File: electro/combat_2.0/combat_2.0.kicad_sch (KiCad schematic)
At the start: 21 parts, among them J1 BATT, J5 UART, SW1 BOOT, SW2 EN, U2 AZ1117CH-5.0TRG1, U6 LD29150DT33R

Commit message: competition rules
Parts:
- added D3: LED, symbol Device:LED
- added R1: 220, Resistor_SMD:R_1206_3216Metric_Pad1.30x1.75mm_HandSolder, symbol Device:R
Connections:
- net +5V: now also C13.1, U6.3 (IN)
- net +8V: no longer C13.1, U6.3 (IN)
- net ESP32 PCB adapter/IO35: now also D3.2 (A)
- net GND: now also R1.1
- new net: D3.1 (K), R1.2
- no-connect marks 20 -> 18
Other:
- note added: "Competition Rules: Robot must include a mechanism allowing to turn off its drive and weapon safely after loosing connection with a transmitter. Robot must be equipped with a clearly visible, durable weapon lock (e.g. a safety pin crippling a blade) Robot must be equipped with ON/OFF state indicator, clearly visible for a referee in any robot's position and orientation (e.g. high power LED)."
- note added: "This Led Should be visible from outside the robot"
- moved on the sheet: J5

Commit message: almost ready pcb
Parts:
- removed C18: 0.1uF, Capacitor_SMD:C_1206_3216Metric_Pad1.33x1.80mm_HandSolder, symbol Device:C
- removed R8: 10kR, Resistor_SMD:R_1206_3216Metric_Pad1.30x1.75mm_HandSolder, symbol Device:R
- added J2: Conn_01x02_Socket, Connector_PinHeader_2.54mm:PinHeader_1x02_P2.54mm_Vertical, symbol Connector:Conn_01x02_Socket
- added R6: 220, Resistor_THT:R_Axial_DIN0204_L3.6mm_D1.6mm_P7.62mm_Horizontal, symbol Device:R
- C2: renamed from C1; value 10uF -> 22uF; footprint Capacitor_SMD:C_1206_3216Metric_Pad1.33x1.80mm_HandSolder -> Capacitor_SMD:C_0805_2012Metric_Pad1.18x1.45mm_HandSolder
- C4: renamed from C2; footprint Capacitor_SMD:C_1206_3216Metric_Pad1.33x1.80mm_HandSolder -> Capacitor_SMD:C_0805_2012Metric_Pad1.18x1.45mm_HandSolder
- C6: renamed from C13; value 0.33uF -> 1uF; footprint Capacitor_SMD:C_1206_3216Metric_Pad1.33x1.80mm_HandSolder -> (none); symbol Device:C -> Device:C_Small
- C7: renamed from C15; footprint Capacitor_SMD:C_1206_3216Metric_Pad1.33x1.80mm_HandSolder -> Capacitor_SMD:C_0805_2012Metric_Pad1.18x1.45mm_HandSolder
- C8: renamed from C14; value 10uF -> 1uF; footprint Capacitor_SMD:CP_Elec_4x5.4 -> Capacitor_SMD:C_0805_2012Metric_Pad1.18x1.45mm_HandSolder; symbol Device:C_Polarized -> Device:C_Small
- D1: renamed from D2; footprint LED_SMD:LED_1206_3216Metric_Pad1.42x1.75mm_HandSolder -> LED_SMD:LED_PLCC-2_3x2mm_AK
- R4: footprint Resistor_SMD:R_1206_3216Metric_Pad1.30x1.75mm_HandSolder -> Resistor_THT:R_Axial_DIN0204_L3.6mm_D1.6mm_P7.62mm_Horizontal
- U2: renamed from U6; footprint Package_TO_SOT_SMD:TO-252-2 -> Package_TO_SOT_SMD:SOT-353_SC-70-5; symbol Regulator_Linear:LD1086DT33TR -> Regulator_Linear:MIC5366-3.3YC5
- renumbered C16 to C1, C17 to C3, D3 to D2, J5 to J3, R10 to R1, R1 to R2, R9 to R3, SW2 to SW1, SW1 to SW2, U2 to U1
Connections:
- net +3V3: now also U2.5 (VOUT), R6.1; no longer U2.2 (OUT)
- net +5V: now also U2.1 (VIN)
- net ESP32 PCB adapter/IO16: now also R6.2
- net ESP32 PCB adapter/IO35: now also J2.2 (Pin_2); no longer D2.2 (A)
- net GND: now also U2.2 (GND); no longer U2.1 (ADJ/GND)
- net at R2.2: now also J2.1 (Pin_1); no longer D2.1 (K)
- no-connect marks 18 -> 12
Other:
- note added: "Chyba można dać po prostu jeden C ?"
- note added: "Chyba można dać po prostu jeden C Jak będą blisko siebie?"
- moved on the sheet: C1, C3, D1, D2, R1, R2, R3, SW1

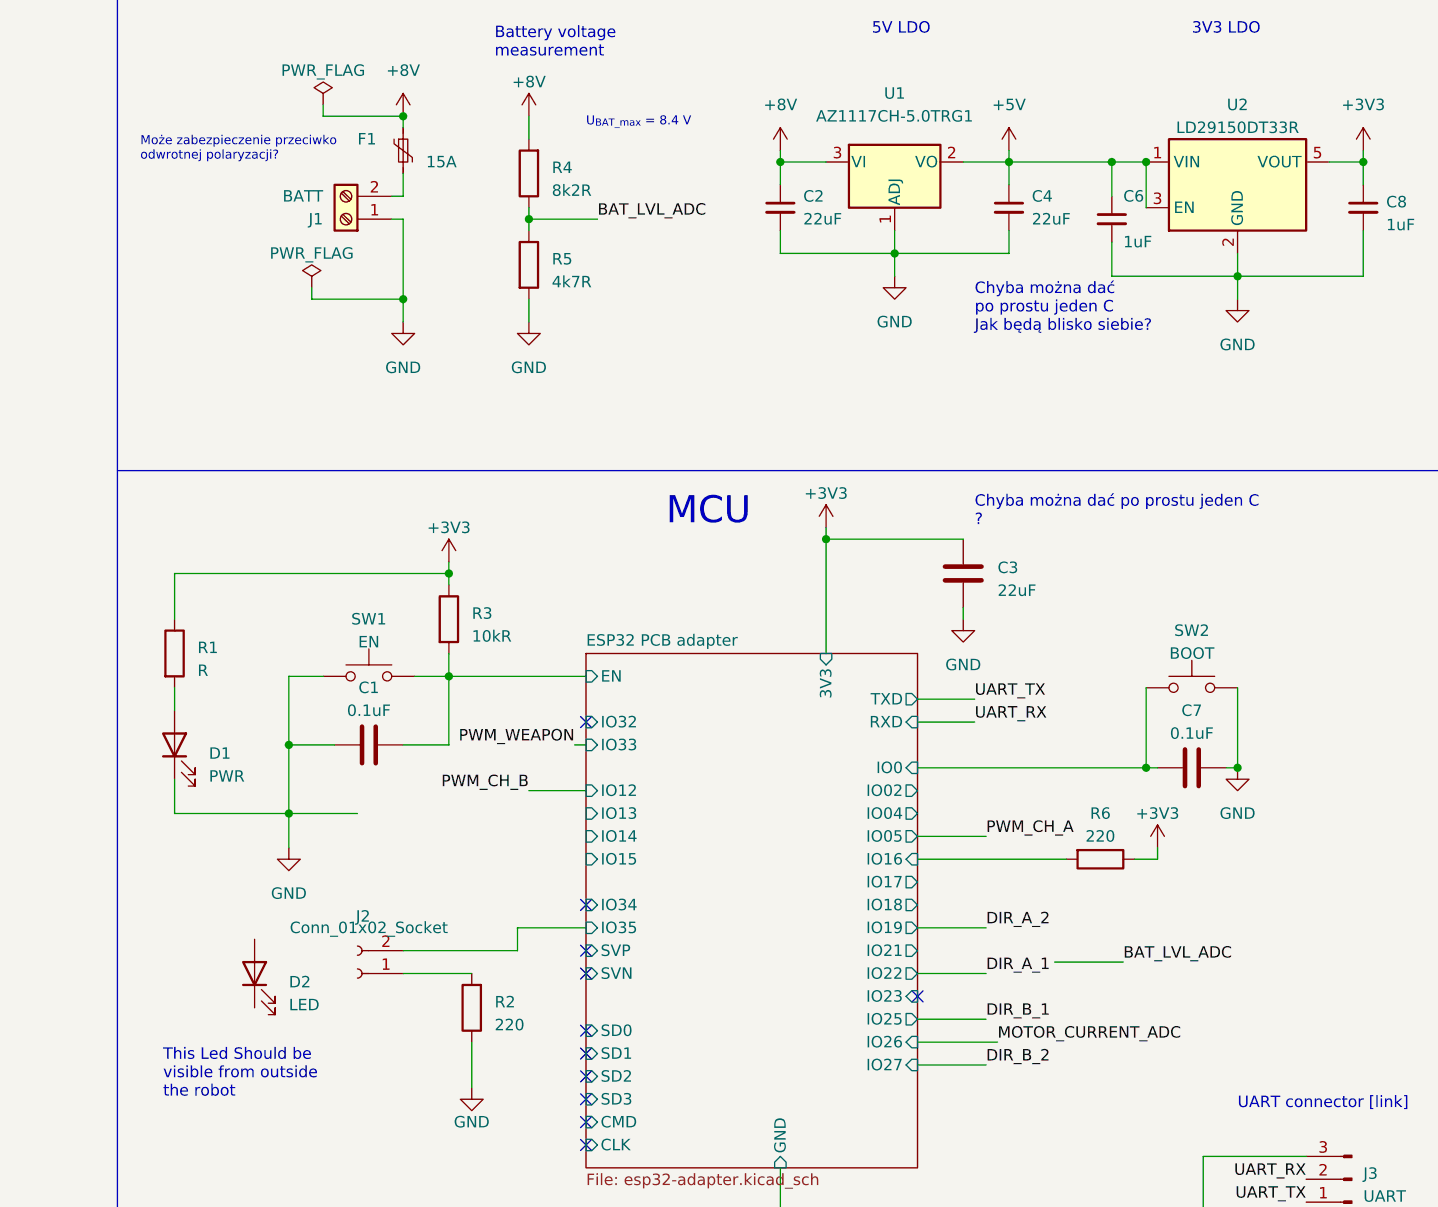
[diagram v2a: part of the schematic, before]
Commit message: Changed pads to ARKs (connecting two boards together), prepared for etching
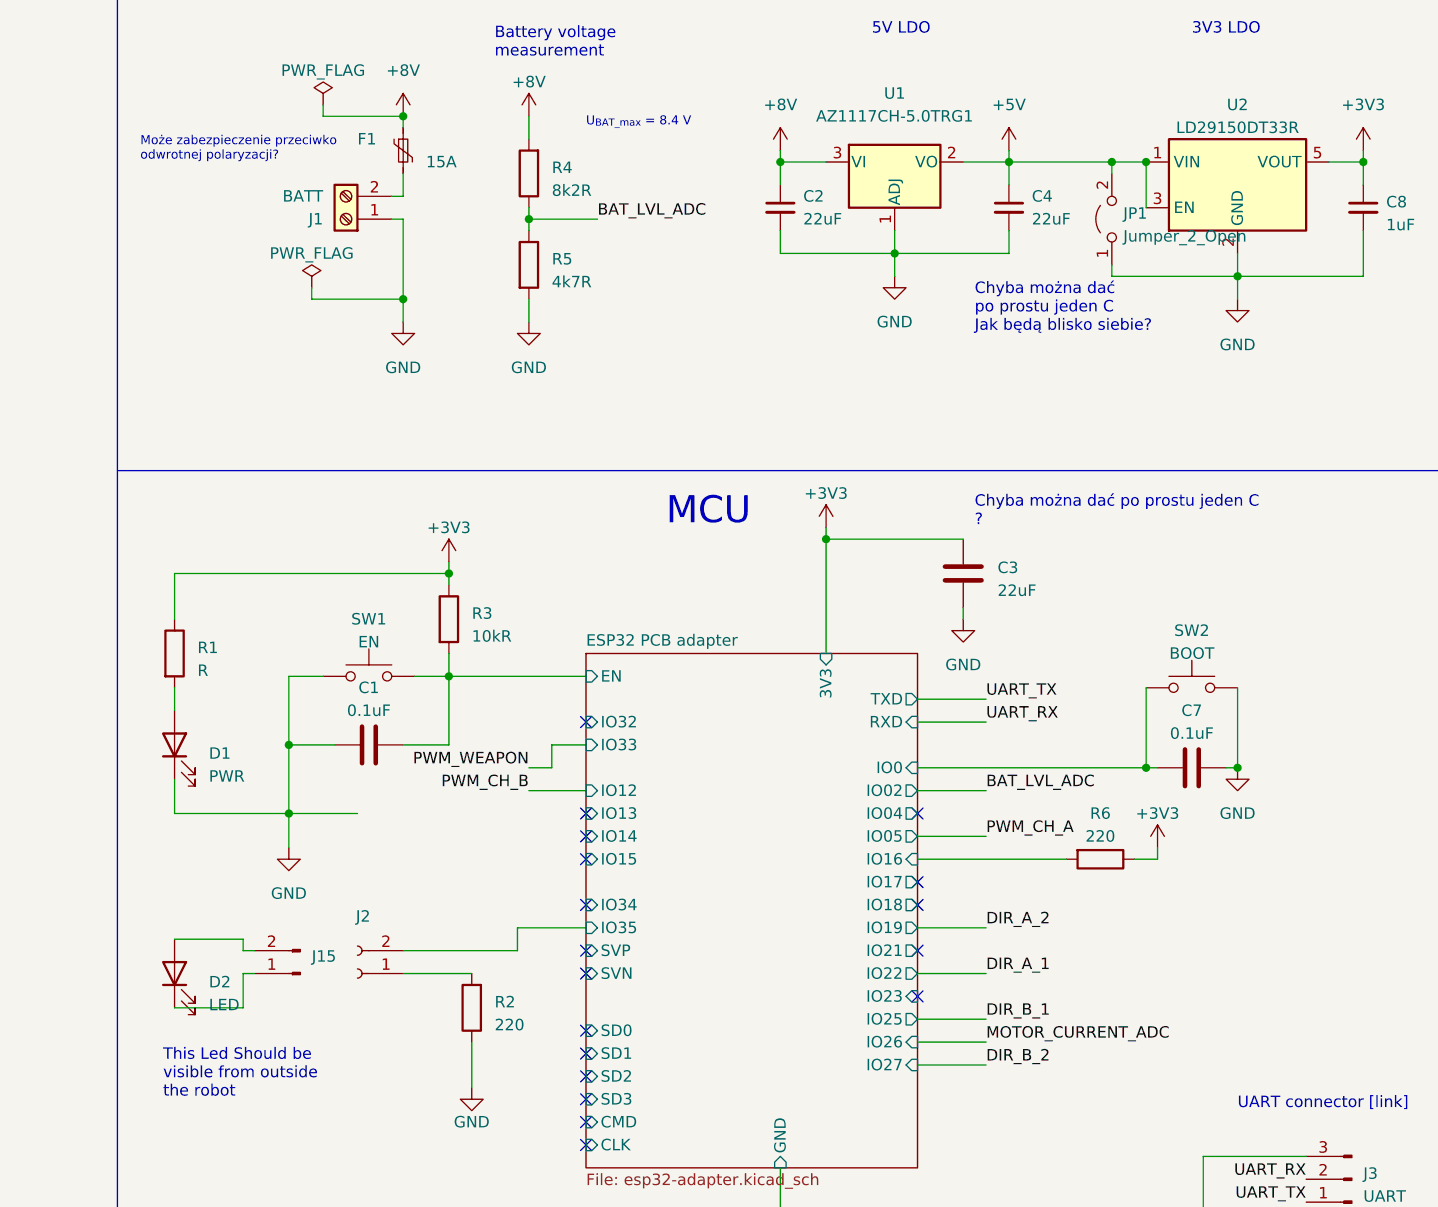
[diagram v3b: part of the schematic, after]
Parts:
- removed C6: 1uF, symbol Device:C_Small
- added J15: Conn_01x02_Pin, symbol Connector:Conn_01x02_Pin
- added JP1: Jumper_2_Open, symbol Jumper:Jumper_2_Open
- R4: footprint Resistor_THT:R_Axial_DIN0204_L3.6mm_D1.6mm_P7.62mm_Horizontal -> Resistor_SMD:R_1206_3216Metric_Pad1.30x1.75mm_HandSolder
- SW1, SW2: now left out of the parts list
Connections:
- net +5V: now also JP1.2 (B)
- net GND: now also JP1.1 (A)
- net at D2.1 (K): now also J15.1 (Pin_1)
- net at D2.2 (A): now also J15.2 (Pin_2)
- no-connect marks 12 -> 19
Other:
- moved on the sheet: D2
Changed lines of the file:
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@@
   (no_connect (at 245.11 48.26))
   (no_connect (at 111.76 147.32))
+  (no_connect (at 74.93 127))
+  (no_connect (at 111.76 127))
   (no_connect (at 74.93 142.24))
   (no_connect (at 74.93 153.67))
@@
   (no_connect (at 74.93 137.16))
   (no_connect (at 74.93 144.78))
+  (no_connect (at 111.76 142.24))
+  (no_connect (at 111.76 134.62))
   (no_connect (at 74.93 163.83))
+  (no_connect (at 74.93 129.54))
+  (no_connect (at 111.76 137.16))
+  (no_connect (at 74.93 132.08))
   (no_connect (at 74.93 151.13))
   (no_connect (at 74.93 156.21))
@@
     (stroke (width 0) (type default))
   )
+  (wire (pts (xy 29.21 148.59) (xy 36.83 148.59))
+    (stroke (width 0) (type default))
+  )
   (wire (pts (xy 212.09 48.26) (xy 204.47 48.26))
     (stroke (width 0) (type default))
@@
     (stroke (width 0) (type default))
   )
-  (wire (pts (xy 111.76 116.84) (xy 118.11 116.84))
+  (wire (pts (xy 111.76 116.84) (xy 119.38 116.84))
     (stroke (width 0) (type default))
   )
@@
     (stroke (width 0) (type default))
   )
-  (wire (pts (xy 127 143.51) (xy 134.62 143.51))
+  (wire (pts (xy 111.76 124.46) (xy 119.38 124.46))
     (stroke (width 0) (type default))
   )
@@
     (stroke (width 0) (type default))
   )
-  (wire (pts (xy 133.35 54.61) (xy 133.35 58.42))
+  (wire (pts (xy 133.35 54.61) (xy 133.35 55.88))
     (stroke (width 0) (type default))
   )
@@
     (stroke (width 0) (type default))
   )
+  (wire (pts (xy 71.12 121.92) (xy 71.12 119.38))
+    (stroke (width 0) (type default))
+  )
   (wire (pts (xy 147.32 67.31) (xy 161.29 67.31))
     (stroke (width 0) (type default))
@@
     (stroke (width 0) (type default))
   )
-  (wire (pts (xy 111.76 152.4) (xy 120.65 152.4))
+  (wire (pts (xy 111.76 152.4) (xy 119.38 152.4))
     (stroke (width 0) (type default))
   )
@@
     (stroke (width 0) (type default))
   )
+  (wire (pts (xy 36.83 144.78) (xy 38.1 144.78))
+    (stroke (width 0) (type default))
+  )
   (wire (pts (xy 242.57 125.73) (xy 245.11 125.73))
     (stroke (width 0) (type default))
@@
     (stroke (width 0) (type default))
   )
-  (wire (pts (xy 133.35 63.5) (xy 133.35 67.31))
-    (stroke (width 0) (type default))
-  )
   (wire (pts (xy 62.23 152.4) (xy 62.23 157.48))
     (stroke (width 0) (type default))
   )
-  (wire (pts (xy 74.93 119.38) (xy 73.66 119.38))
+  (wire (pts (xy 71.12 121.92) (xy 68.58 121.92))
     (stroke (width 0) (type default))
   )
@@
     (stroke (width 0) (type default))
   )
+  (wire (pts (xy 29.21 140.97) (xy 36.83 140.97))
+    (stroke (width 0) (type default))
+  )
   (polyline (pts (xy 274.32 157.48) (xy 274.32 19.05))
     (stroke (width 0) (type default))
@@
     (stroke (width 0) (type default))
   )
+  (wire (pts (xy 36.83 142.24) (xy 38.1 142.24))
+    (stroke (width 0) (type default))
+  )
   (wire (pts (xy 111.76 132.08) (xy 128.27 132.08))
     (stroke (width 0) (type default))
@@
     (stroke (width 0) (type default))
   )
+  (wire (pts (xy 133.35 66.04) (xy 133.35 67.31))
+    (stroke (width 0) (type default))
+  )
   (wire (pts (xy 205.74 133.35) (xy 205.74 137.16))
     (stroke (width 0) (type default))
   )
+  (wire (pts (xy 36.83 148.59) (xy 36.83 144.78))
+    (stroke (width 0) (type default))
+  )
   (wire (pts (xy 241.3 55.88) (xy 243.84 55.88))
     (stroke (width 0) (type default))
   )
-  (wire (pts (xy 111.76 114.3) (xy 118.11 114.3))
+  (wire (pts (xy 111.76 114.3) (xy 119.38 114.3))
     (stroke (width 0) (type default))
   )
@@
   )
   (wire (pts (xy 111.76 129.54) (xy 119.38 129.54))
+    (stroke (width 0) (type default))
+  )
+  (wire (pts (xy 71.12 119.38) (xy 74.93 119.38))
+    (stroke (width 0) (type default))
+  )
+  (wire (pts (xy 36.83 140.97) (xy 36.83 142.24))
     (stroke (width 0) (type default))
   )
@@
     (effects (font (size 1.27 1.27)) (justify left bottom))
   )
-  (label "UART_RX" (at 118.11 116.84 0) (fields_autoplaced)
+  (label "UART_RX" (at 119.38 116.84 0) (fields_autoplaced)
     (effects (font (size 1.27 1.27)) (justify left bottom))
   )
@@
     (effects (font (size 1.27 1.27)) (justify left bottom))
   )
-  (label "MOTOR_CURRENT_ADC" (at 120.65 152.4 0) (fields_autoplaced)
-    (effects (font (size 1.27 1.27)) (justify left bottom))
-  )
-  (label "BAT_LVL_ADC" (at 134.62 143.51 0) (fields_autoplaced)
+  (label "MOTOR_CURRENT_ADC" (at 119.38 152.4 0) (fields_autoplaced)
+    (effects (font (size 1.27 1.27)) (justify left bottom))
+  )
+  (label "BAT_LVL_ADC" (at 119.38 124.46 0) (fields_autoplaced)
     (effects (font (size 1.27 1.27)) (justify left bottom))
   )
@@
     (effects (font (size 1.27 1.27)) (justify left bottom))
   )
-  (label "PWM_WEAPON" (at 73.66 119.38 180) (fields_autoplaced)
+  (label "PWM_WEAPON" (at 68.58 121.92 180) (fields_autoplaced)
     (effects (font (size 1.27 1.27)) (justify right bottom))
   )
-  (label "UART_TX" (at 118.11 114.3 0) (fields_autoplaced)
+  (label "UART_TX" (at 119.38 114.3 0) (fields_autoplaced)
     (effects (font (size 1.27 1.27)) (justify left bottom))
   )
@@
       (effects (font (size 1.27 1.27)) (justify right))
     )
-    (property "Footprint" "Resistor_THT:R_Axial_DIN0204_L3.6mm_D1.6mm_P7.62mm_Horizontal" (at 70.358 55.88 90)
+    (property "Footprint" "Resistor_SMD:R_1206_3216Metric_Pad1.30x1.75mm_HandSolder" (at 70.358 55.88 90)
       (effects (font (size 1.27 1.27)) hide)
     )
@@
   )
   (symbol (lib_id "Switch:SW_Push") (at 50.8 111.76 0) (unit 1)
-    (in_bom yes) (on_board yes) (dnp no) (fields_autoplaced)
+    (in_bom no) (on_board no) (dnp no) (fields_autoplaced)
     (property "Reference" "SW1" (at 50.8 105.41 0)
       (effects (font (size 1.27 1.27)))
@@
     )
   )
+  (symbol (lib_id "Jumper:Jumper_2_Open") (at 133.35 60.96 90) (unit 1)
+    (in_bom no) (on_board no) (dnp no) (fields_autoplaced)
+    (property "Reference" "JP1" (at 134.62 60.325 90)
+      (effects (font (size 1.27 1.27)) (justify right))
+    )
+    (property "Value" "Jumper_2_Open" (at 134.62 62.865 90)
+      (effects (font (size 1.27 1.27)) (justify right))
+    )
+    (property "Footprint" "" (at 133.35 60.96 0)
+      (effects (font (size 1.27 1.27)) hide)
+    )
+    (property "Datasheet" "~" (at 133.35 60.96 0)
+      (effects (font (size 1.27 1.27)) hide)
+    )
+    (pin "1")
+    (pin "2")
+    (instances
+      (project "combat_2.0"
+        (path "/518cdd36-e3d2-496e-a534-90a14dea15b3"
+          (reference "JP1") (unit 1)
+        )
+      )
+    )
+  )
   (symbol (lib_id "Device:C") (at 142.24 121.92 90) (unit 1)
     (in_bom yes) (on_board yes) (dnp no) (fields_autoplaced)
@@
     )
   )
+  (symbol (lib_id "Connector:Conn_01x02_Pin") (at 43.18 144.78 180) (unit 1)
+    (in_bom no) (on_board no) (dnp no) (fields_autoplaced)
+    (property "Reference" "J15" (at 44.45 142.875 0)
+      (effects (font (size 1.27 1.27)) (justify right))
+    )
+    (property "Value" "Conn_01x02_Pin" (at 44.45 145.415 0)
+      (effects (font (size 1.27 1.27)) (justify right) hide)
+    )
+    (property "Footprint" "" (at 43.18 144.78 0)
+      (effects (font (size 1.27 1.27)) hide)
+    )
+    (property "Datasheet" "~" (at 43.18 144.78 0)
+      (effects (font (size 1.27 1.27)) hide)
+    )
+    (pin "1")
+    (pin "2")
+    (instances
+      (project "combat_2.0"
+        (path "/518cdd36-e3d2-496e-a534-90a14dea15b3"
+          (reference "J15") (unit 1)
+        )
+      )
+    )
+  )
   (symbol (lib_id "power:GND") (at 116.84 105.41 0) (unit 1)
     (in_bom yes) (on_board yes) (dnp no) (fields_autoplaced)
@@
     )
   )
-  (symbol (lib_id "Device:C_Small") (at 133.35 60.96 0) (unit 1)
-    (in_bom yes) (on_board yes) (dnp no)
-    (property "Reference" "C6" (at 134.62 58.42 0)
-      (effects (font (size 1.27 1.27)) (justify left))
-    )
-    (property "Value" "1uF" (at 134.62 63.5 0)
-      (effects (font (size 1.27 1.27)) (justify left))
-    )
-    (property "Footprint" "" (at 133.35 60.96 0)
-      (effects (font (size 1.27 1.27)) hide)
-    )
-    (property "Datasheet" "~" (at 133.35 60.96 0)
-      (effects (font (size 1.27 1.27)) hide)
-    )
-    (pin "1")
-    (pin "2")
-    (instances
-      (project "combat_2.0"
-        (path "/518cdd36-e3d2-496e-a534-90a14dea15b3"
-          (reference "C6") (unit 1)
-        )
-      )
-    )
-  )
   (symbol (lib_id "power:PWR_FLAG") (at 44.45 68.58 0) (unit 1)
     (in_bom yes) (on_board yes) (dnp no) (fields_autoplaced)
@@
   )
   (symbol (lib_id "Switch:SW_Push") (at 142.24 113.03 0) (unit 1)
-    (in_bom yes) (on_board yes) (dnp no) (fields_autoplaced)
+    (in_bom no) (on_board no) (dnp no) (fields_autoplaced)
     (property "Reference" "SW2" (at 142.24 106.68 0)
       (effects (font (size 1.27 1.27)))
@@
     )
   )
-  (symbol (lib_id "Device:LED") (at 38.1 144.78 90) (unit 1)
-    (in_bom yes) (on_board yes) (dnp no) (fields_autoplaced)
-    (property "Reference" "D2" (at 41.91 145.7325 90)
+  (symbol (lib_id "Device:LED") (at 29.21 144.78 90) (unit 1)
+    (in_bom yes) (on_board no) (dnp no) (fields_autoplaced)
+    (property "Reference" "D2" (at 33.02 145.7325 90)
       (effects (font (size 1.27 1.27)) (justify right))
     )
-    (property "Value" "LED" (at 41.91 148.2725 90)
+    (property "Value" "LED" (at 33.02 148.2725 90)
       (effects (font (size 1.27 1.27)) (justify right))
     )
-    (property "Footprint" "" (at 38.1 144.78 0)
-      (effects (font (size 1.27 1.27)) hide)
-    )
-    (property "Datasheet" "~" (at 38.1 144.78 0)
+    (property "Footprint" "" (at 29.21 144.78 0)
+      (effects (font (size 1.27 1.27)) hide)
+    )
+    (property "Datasheet" "~" (at 29.21 144.78 0)
       (effects (font (size 1.27 1.27)) hide)
     )
@@
     )
     (property "Value" "Conn_01x02_Socket" (at 50.8 139.7 0)
-      (effects (font (size 1.27 1.27)))
+      (effects (font (size 1.27 1.27)) hide)
     )
     (property "Footprint" "Connector_PinHeader_2.54mm:PinHeader_1x02_P2.54mm_Vertical" (at 49.53 144.78 0)

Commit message: Change in mosfets routing
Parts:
- C1, C3: footprint Capacitor_SMD:C_1206_3216Metric_Pad1.33x1.80mm_HandSolder -> Capacitor_SMD:C_0805_2012Metric_Pad1.18x1.45mm_HandSolder
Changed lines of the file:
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@@
       (effects (font (size 1.27 1.27)) (justify left))
     )
-    (property "Footprint" "Capacitor_SMD:C_1206_3216Metric_Pad1.33x1.80mm_HandSolder" (at 117.8052 104.14 0)
+    (property "Footprint" "Capacitor_SMD:C_0805_2012Metric_Pad1.18x1.45mm_HandSolder" (at 117.8052 104.14 0)
       (effects (font (size 1.27 1.27)) hide)
     )
@@
       (effects (font (size 1.27 1.27)))
     )
-    (property "Footprint" "Capacitor_SMD:C_1206_3216Metric_Pad1.33x1.80mm_HandSolder" (at 54.61 118.4148 0)
-      (effects (font (size 1.27 1.27)) hide)
-    )
+    (property "Footprint" "Capacitor_SMD:C_0805_2012Metric_Pad1.18x1.45mm_HandSolder" (at 54.61 118.4148 0)
+      (effects (font (size 1.27 1.27)) hide)
+    )
